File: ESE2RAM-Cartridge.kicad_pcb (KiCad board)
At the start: 2 copper layers, 100 x 60.5 mm, 27 parts, among them CN1 BUS_MSX, IC1 4M SRAM, IC2 4M SRAM, J1 8M, U1 74HC670, U2 74HC670, U3 74AHC138, U4 74AHC00, U5 74AHC32

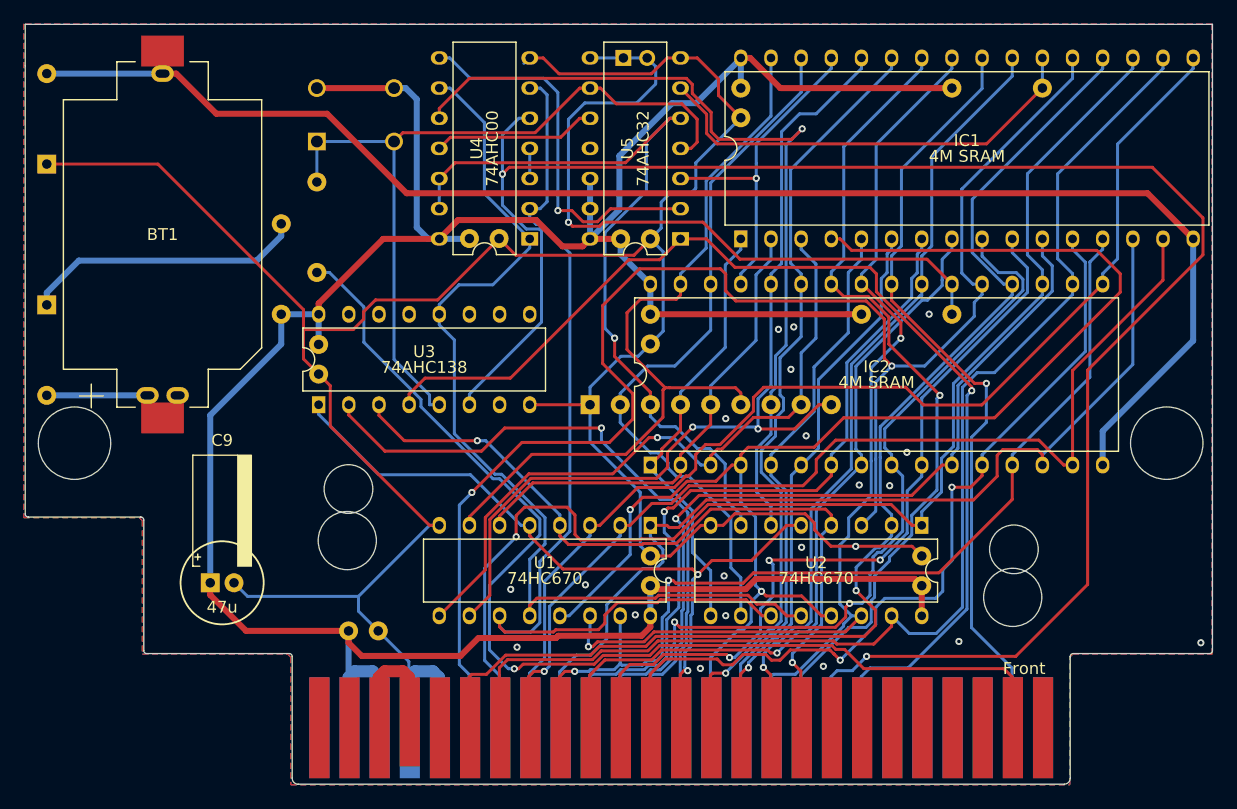
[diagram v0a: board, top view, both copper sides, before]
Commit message: Updated schematic revision.
バックアップ電源回路を改良しました
Backup power supply circuit has been refined.
カートリッジ無効化スイッチを改良しました
Cartridge deactivation switch has been refined.
アドレスデコーダを改良しました
Address decoder has been refined.
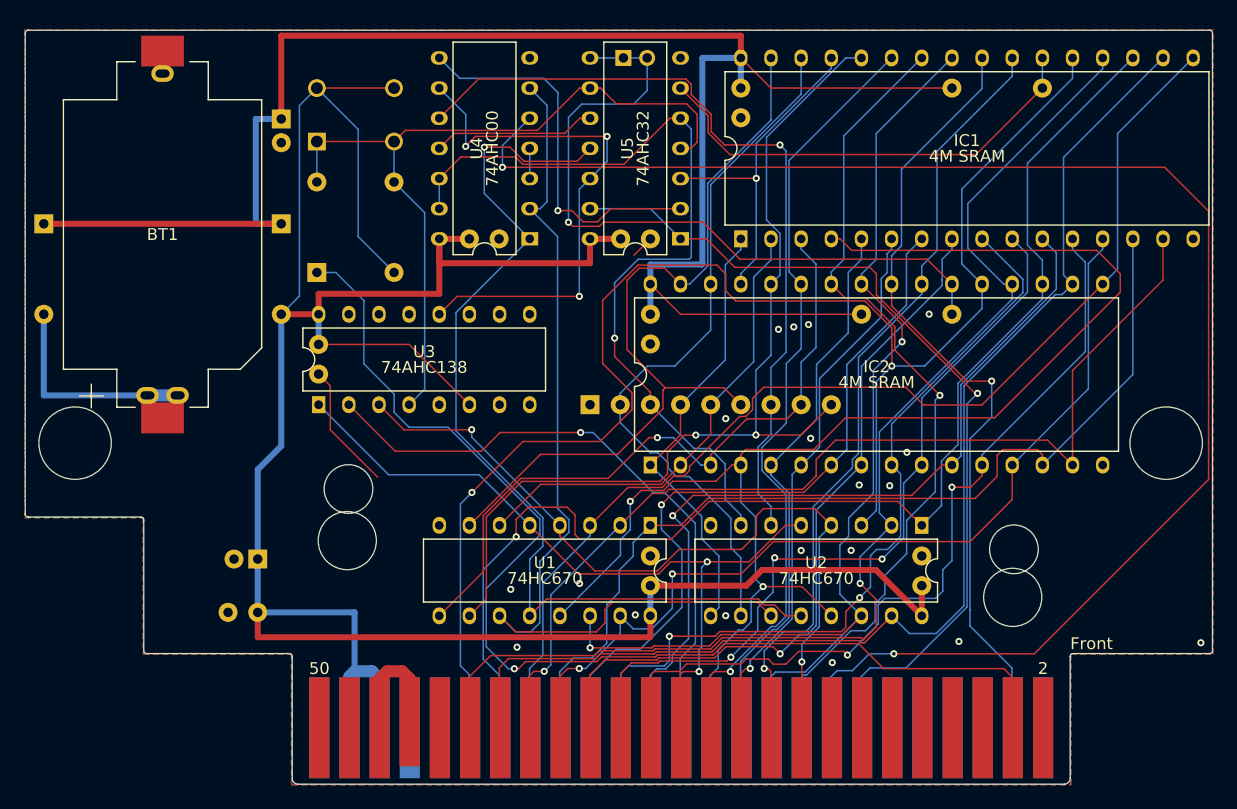
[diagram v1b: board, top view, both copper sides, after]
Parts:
- removed R4: 10K, Resistor_THT:R_Axial_DIN0207_L6.3mm_D2.5mm_P7.62mm_Horizontal
- added C10: 47u, ProjectLibrary:CP_Radial_D5.0mm_P2.00mm_Horizontal, B.Cu at (61.4, 107.3)
- added D3: BAT43, Diode_THT:D_DO-35_SOD27_P7.62mm_Horizontal, B.Cu at (64.4, 120.3)
- C9: moved to B.Cu
- CN1: footprint ProjectLibrary:BUS_MSX_CARD_SHORT -> ProjectLibrary:CARD_MSX_AK_DUAL
- D1, D2: value 1N4148 -> BAT43
- R3: value 10K -> 3.3K
- RN1: value 10k -> 10K
- S1: value DTS-63N-V -> TVDP01-095BB1; footprint ProjectLibrary:DTS63NV -> _GoriponsoftLibrary:TVDP01-095BB1
- moved D1 20.4 mm to (61.4, 116.2), turned to -90 degrees
- moved C8 10.3 mm to (59.4, 148.9)
- moved D2 6.83 mm to (41.4, 116.2)
- moved R3 6.50 mm to (70.9, 112.6)
- moved C9 4.47 mm to (59.4, 144.4), turned to 180 degrees
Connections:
- BT1 pad 2: /BATT- -> GND
- C6 pad 1: +5V -> VDD
- C7 pad 1: +5V -> VDD
- C8 pad 1: GND -> +5V
- C8 pad 2: +5V -> GND
- D1 pad 1: GND -> VDD
- D1 pad 2: /BATT- -> +5V
- D2 pad 1: Net-(D2-K) -> VDD
- IC1 pad 16: /BATT- -> GND
- IC1 pad 32: +5V -> VDD
- IC2 pad 16: /BATT- -> GND
- IC2 pad 32: +5V -> VDD
- R1 pad 2: +5V -> VDD
- R2 pad 2: +5V -> VDD
- R3 pad 1: /~{SLOTSELECT} -> /~{SLTSL^{inner}}
- R3 pad 2: /~{SLTSL} -> +5V
- S1 pad 1: /~{SLOTSELECT} -> /~{SLTSL^{inner}}
- S1 pad 2: /~{SLOTSELECT} -> /~{SLTSL^{inner}}
- U3 pad 12: Net-(U1-~{Ew}) -> Net-(U3-~{Y3})
- U3 pad 4: /~{WR} -> /~{SLTSL^{inner}}
- U3 pad 5: /~{SLOTSELECT} -> GND
- U3 pad 6: /~{RESET} -> +5V
- U4 pad 9: Net-(U1-~{Ew}) -> Net-(U3-~{Y3})
- U5 pad 11: unconnected-(U5-Pad11) -> Net-(U1-~{Ew})
- U5 pad 12: +5V -> Net-(U3-~{Y3})
- U5 pad 13: +5V -> /~{WR}
- U5 pad 4: /~{SLOTSELECT} -> /~{SLTSL^{inner}}
- U5 pad 9: /~{SLOTSELECT} -> /~{SLTSL^{inner}}
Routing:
- net GND: track 228.9 -> 13.0 mm, vias 21 -> 19
- net VDD: track 0.00 -> 150.1 mm
- net /BATT-: track 124.5 -> 0.00 mm
- net /~{SLOTSELECT}: track 66.2 -> 0.00 mm
- net /~{SLTSL^{inner}}: track 0.00 -> 66.0 mm
- net Net-(U3-~{Y3}): track 0.00 -> 45.1 mm, vias 0 -> 3
- net +5V: track 250.0 -> 221.4 mm
- net Net-(D2-K): track 23.8 -> 0.00 mm
- net /~{RESET}: track 155.2 -> 131.7 mm
- net /~{WR}: track 94.2 -> 74.1 mm
- net Net-(BT1-+): track 9.73 -> 24.2 mm
- net /EN_WR: track 71.8 -> 67.4 mm
- net /D0: track 81.4 -> 77.2 mm
- net /~{SLTSL}: track 93.1 -> 95.4 mm
- net /RAM_A19: track 68.5 -> 70.5 mm
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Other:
- board size 100 x 60.5 mm -> 100 x 63.5 mm
- board text added: "似非²RAM rev.7 Goripon Hardware"
- board text removed: "JLCJLCJLCJLC"
- board text removed: "似非²RAM rev.6 Goripon Hardware"

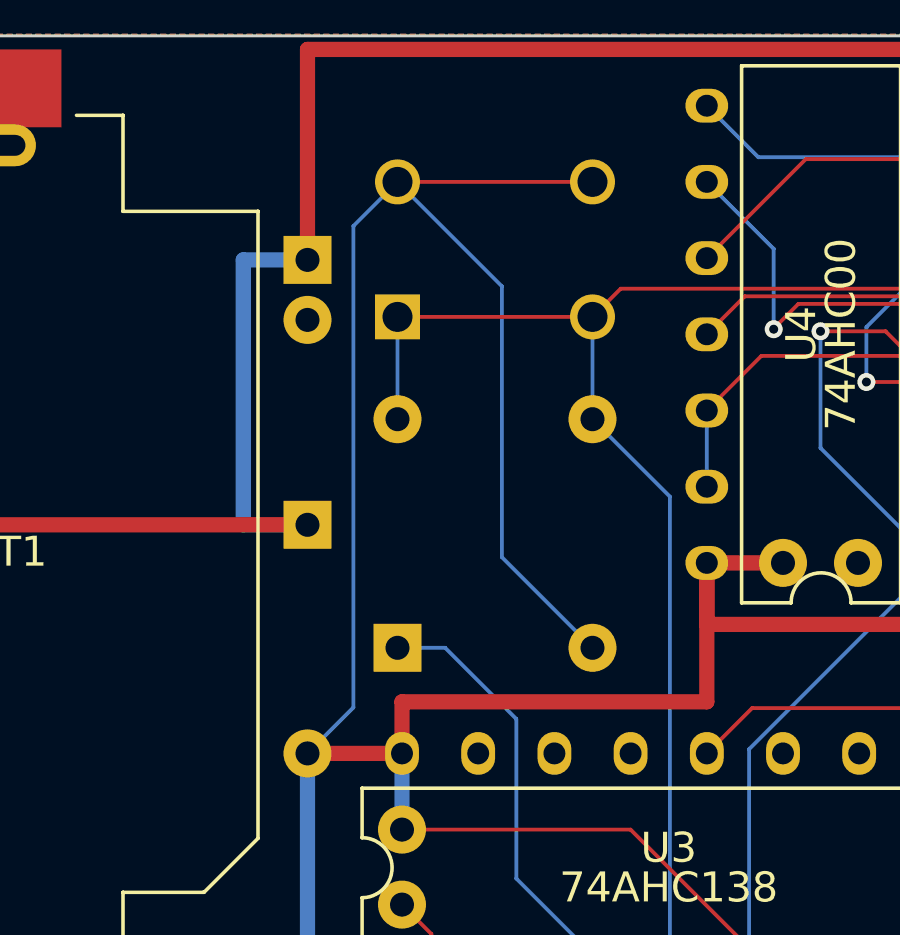
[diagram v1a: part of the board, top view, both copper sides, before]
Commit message: Schematic data correction and addition of documentation.
カートリッジ無効化ボタン周りの改修でコンデンサの追加を忘れていたので修正。
I forgot to add a capacitor when modifying the area around the cartridge disable button, so I fixed that.
基板改修情報のドキュメントを追加。
Added a document titled "Circuit Board Modification Information".
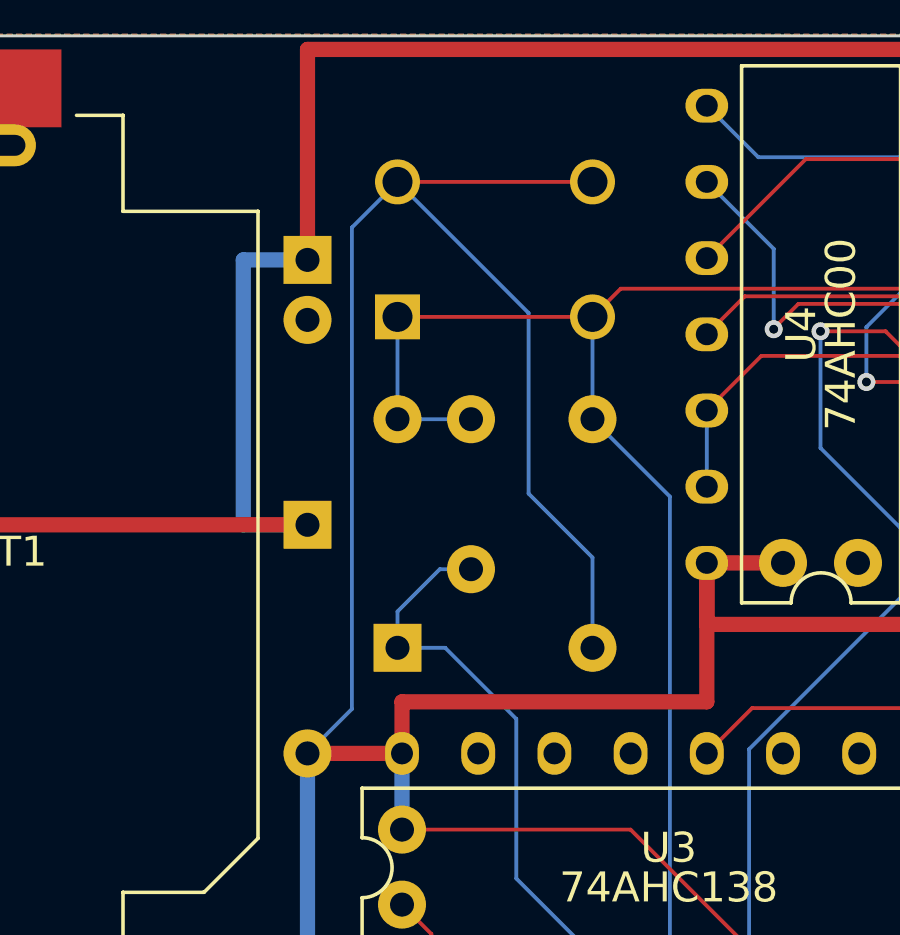
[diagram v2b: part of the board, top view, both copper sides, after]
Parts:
- added C11: 47u, ProjectLibrary:CP_Radial_D5.0mm_P2.00mm_Horizontal, B.Cu at (59.4, 144.4)
- C9: value 47u -> 100p; footprint ProjectLibrary:CP_Radial_D5.0mm_P2.00mm_Horizontal -> Capacitor_THT:C_Disc_D4.3mm_W1.9mm_P5.00mm
- RN1: value 10K -> 10k
- moved C9 27.8 mm to (66.8, 117.6), turned to 90 degrees
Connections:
- C9 pad 1: +5V -> /~{SLTSL}
- C9 pad 2: GND -> /~{SLTSL^{inner}}
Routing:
- net /~{SLTSL}: track 95.4 -> 99.7 mm
- net /~{SLTSL^{inner}}: track 66.0 -> 68.4 mm

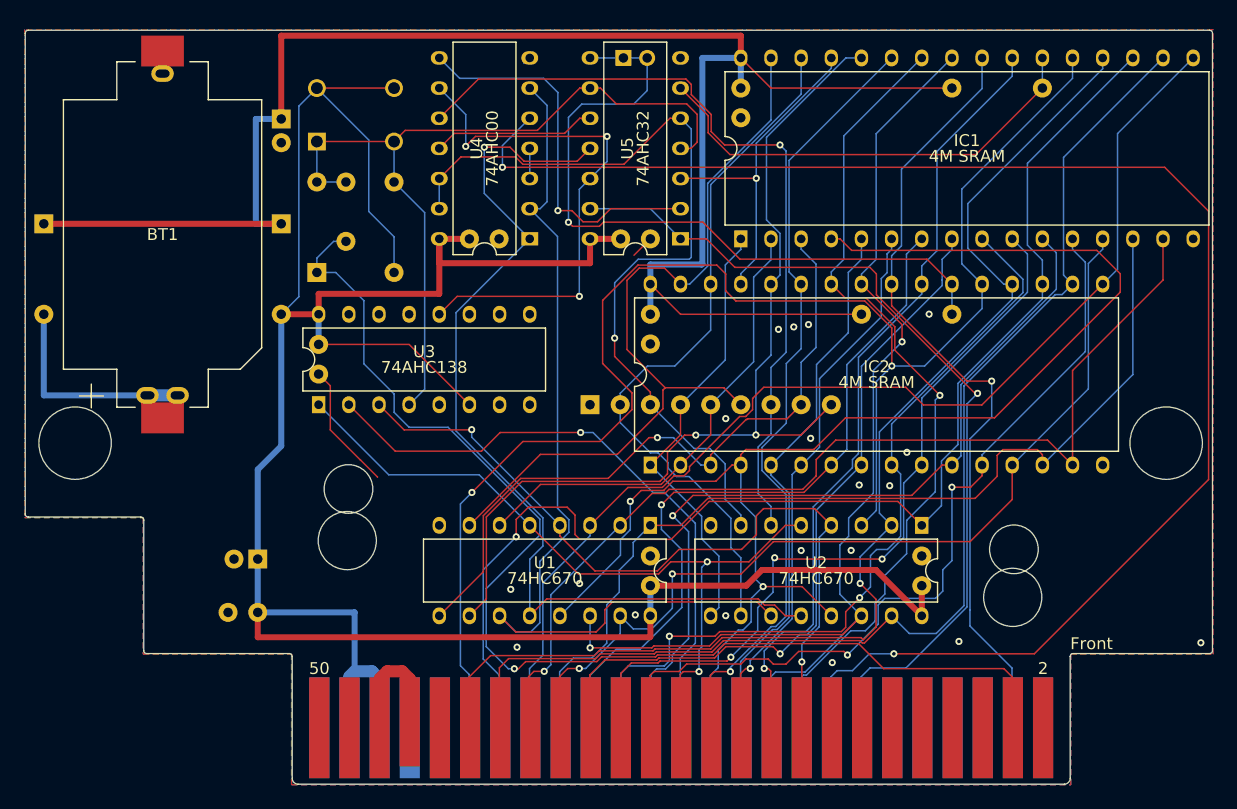
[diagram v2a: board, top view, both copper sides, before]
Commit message: Correction of Schematic data and documents.
アドレスデコード結果を反映させる対象がSRAMの/WE信号から/CE信号に変更された。
The target to which the address decoding results are reflected has been changed from the SRAM's /WE signal to the /CE signal.
基板改修情報のドキュメントを回路図に合わせ修正。
The documentation for circuit board modification information has been revised to match the schematic.
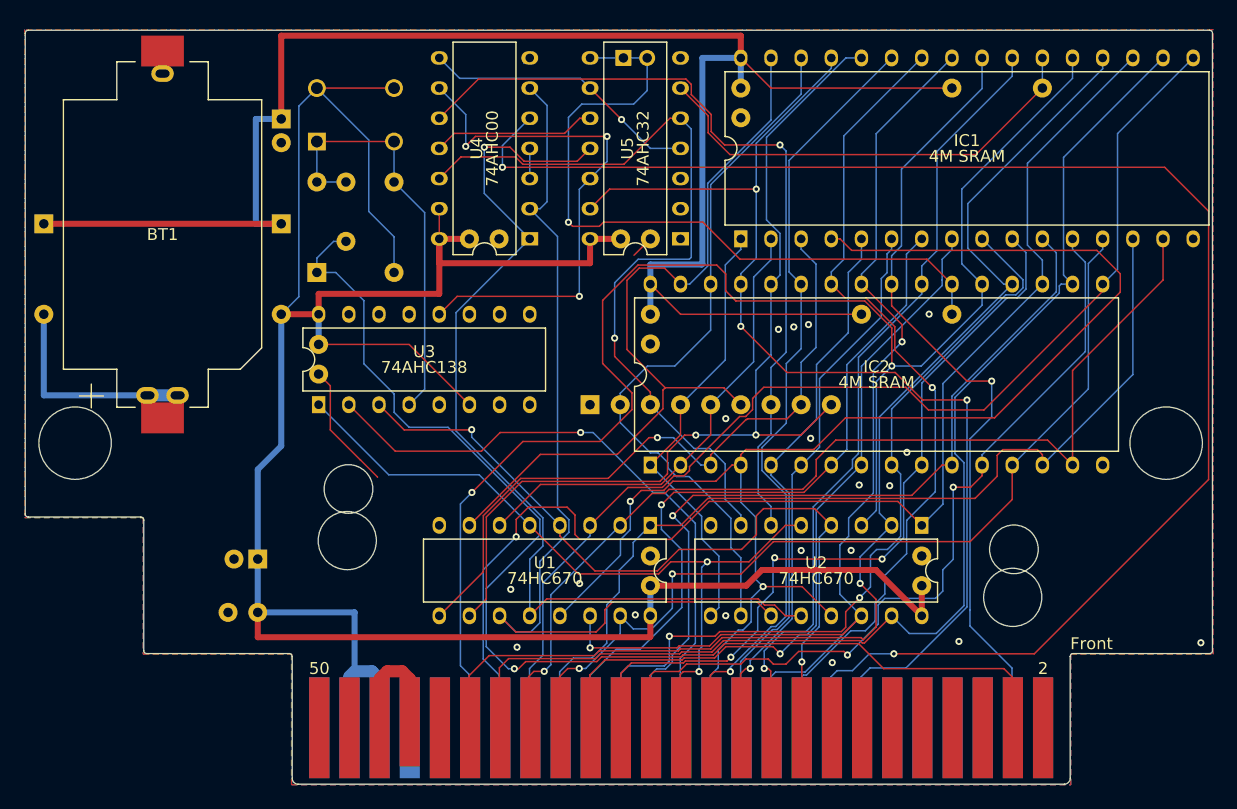
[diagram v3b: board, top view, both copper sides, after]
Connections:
- IC1 pad 29: /~{RAM_WE} -> /~{WR}
- IC2 pad 29: /~{RAM_WE} -> /~{WR}
- U4 pad 13: /RAM_A19 -> +5V
- U4 pad 8: Net-(U4-Pad8) -> /~{RAM_CE}
- U5 pad 1: /~{WR} -> GND
- U5 pad 2: Net-(U4-Pad8) -> GND
- U5 pad 3: /~{RAM_WE} -> unconnected-(U5-Pad3)
- U5 pad 4: /~{SLTSL^{inner}} -> /~{RAM_CE}
- U5 pad 9: /~{SLTSL^{inner}} -> /~{RAM_CE}
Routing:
- net Net-(U4-Pad8): track 32.3 -> 0.00 mm, vias 1 -> 0
- net /~{SLTSL^{inner}}: track 68.4 -> 36.1 mm
- net /~{RAM_WE}: track 28.6 -> 0.00 mm, vias 1 -> 0
- net /~{RAM_CE}: track 0.00 -> 23.5 mm, vias 0 -> 1
- net /~{WR}: track 74.1 -> 95.1 mm, vias 1 -> 3
- net +5V: track 221.4 -> 224.0 mm
- net /RAM_A19: track 70.5 -> 68.0 mm
- net /D4: track 101.8 -> 102.7 mm
- net /D3: track 94.9 -> 95.6 mm

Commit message: Revert "Correction of Schematic data and documents."
This reverts commit bc8d3cb6dc4d5604d2b0a5969a538fbe96077484.
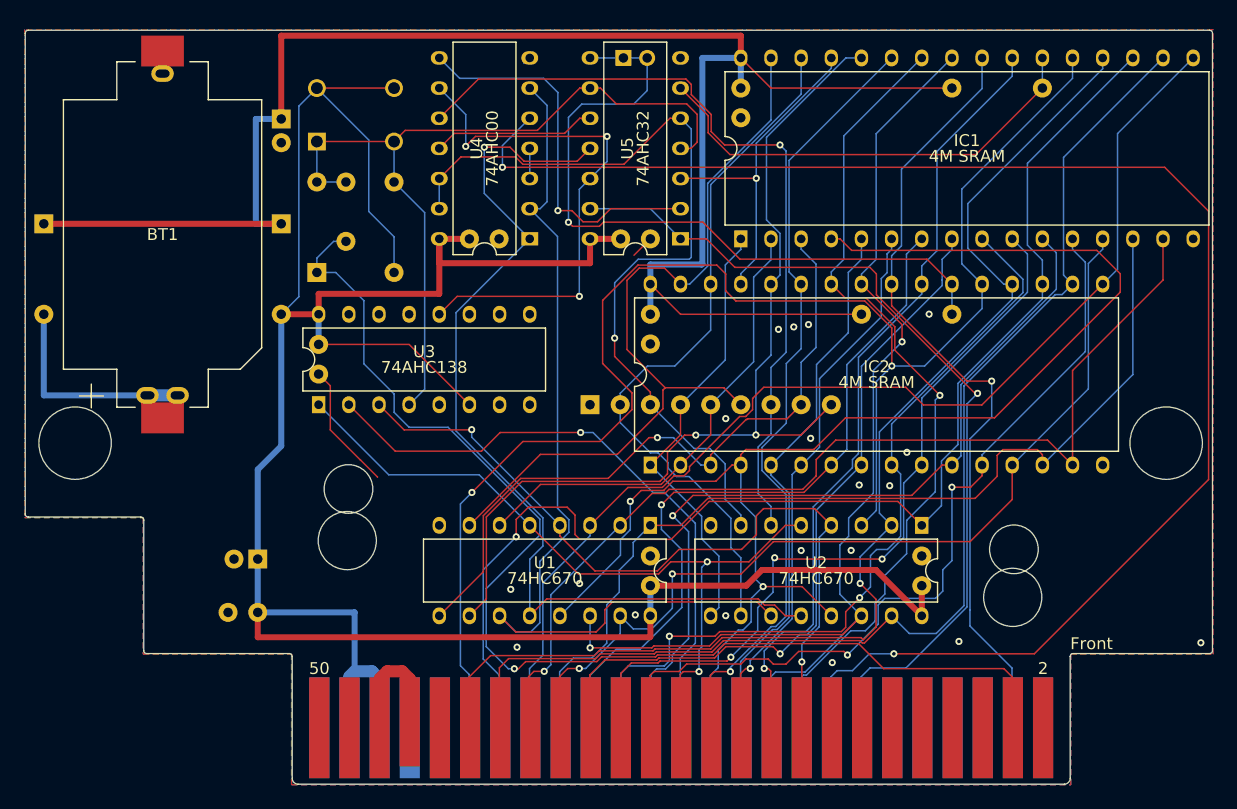
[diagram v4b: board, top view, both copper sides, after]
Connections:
- IC1 pad 29: /~{WR} -> /~{RAM_WE}
- IC2 pad 29: /~{WR} -> /~{RAM_WE}
- U4 pad 13: +5V -> /RAM_A19
- U4 pad 8: /~{RAM_CE} -> Net-(U4-Pad8)
- U5 pad 1: GND -> /~{WR}
- U5 pad 2: GND -> Net-(U4-Pad8)
- U5 pad 3: unconnected-(U5-Pad3) -> /~{RAM_WE}
- U5 pad 4: /~{RAM_CE} -> /~{SLTSL^{inner}}
- U5 pad 9: /~{RAM_CE} -> /~{SLTSL^{inner}}
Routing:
- net Net-(U4-Pad8): track 0.00 -> 32.3 mm, vias 0 -> 1
- net /~{SLTSL^{inner}}: track 36.1 -> 68.4 mm
- net /~{RAM_WE}: track 0.00 -> 28.6 mm, vias 0 -> 1
- net /~{RAM_CE}: track 23.5 -> 0.00 mm, vias 1 -> 0
- net /~{WR}: track 95.1 -> 74.1 mm, vias 3 -> 1
- net +5V: track 224.0 -> 221.4 mm
- net /RAM_A19: track 68.0 -> 70.5 mm
- net /D4: track 102.7 -> 101.8 mm
- net /D3: track 95.6 -> 94.9 mm
